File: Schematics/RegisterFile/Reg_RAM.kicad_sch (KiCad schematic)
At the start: 4 parts, among them U10 IS61WV6416DBLL-10TLI, U11 IS61WV6416DBLL-10TLI, U12 IS61WV6416DBLL-10TLI, U9 IS61WV6416DBLL-10TLI

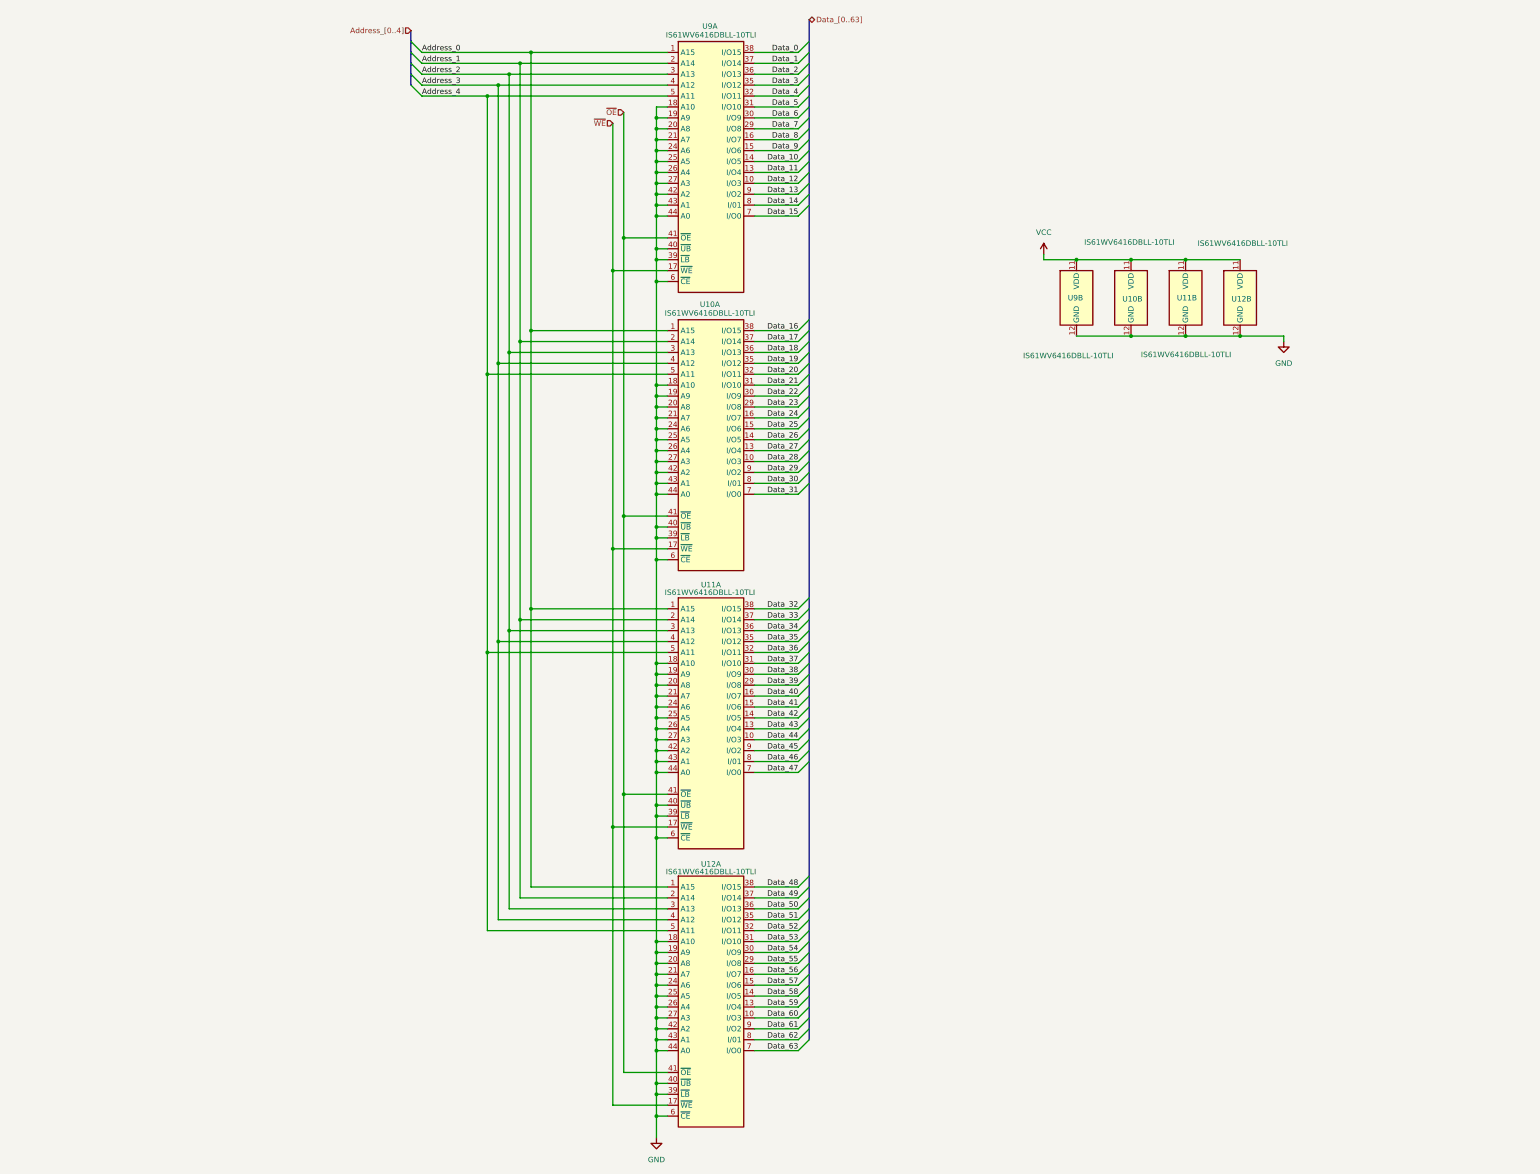
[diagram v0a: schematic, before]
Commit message: Updated RegFile diagrams + timing
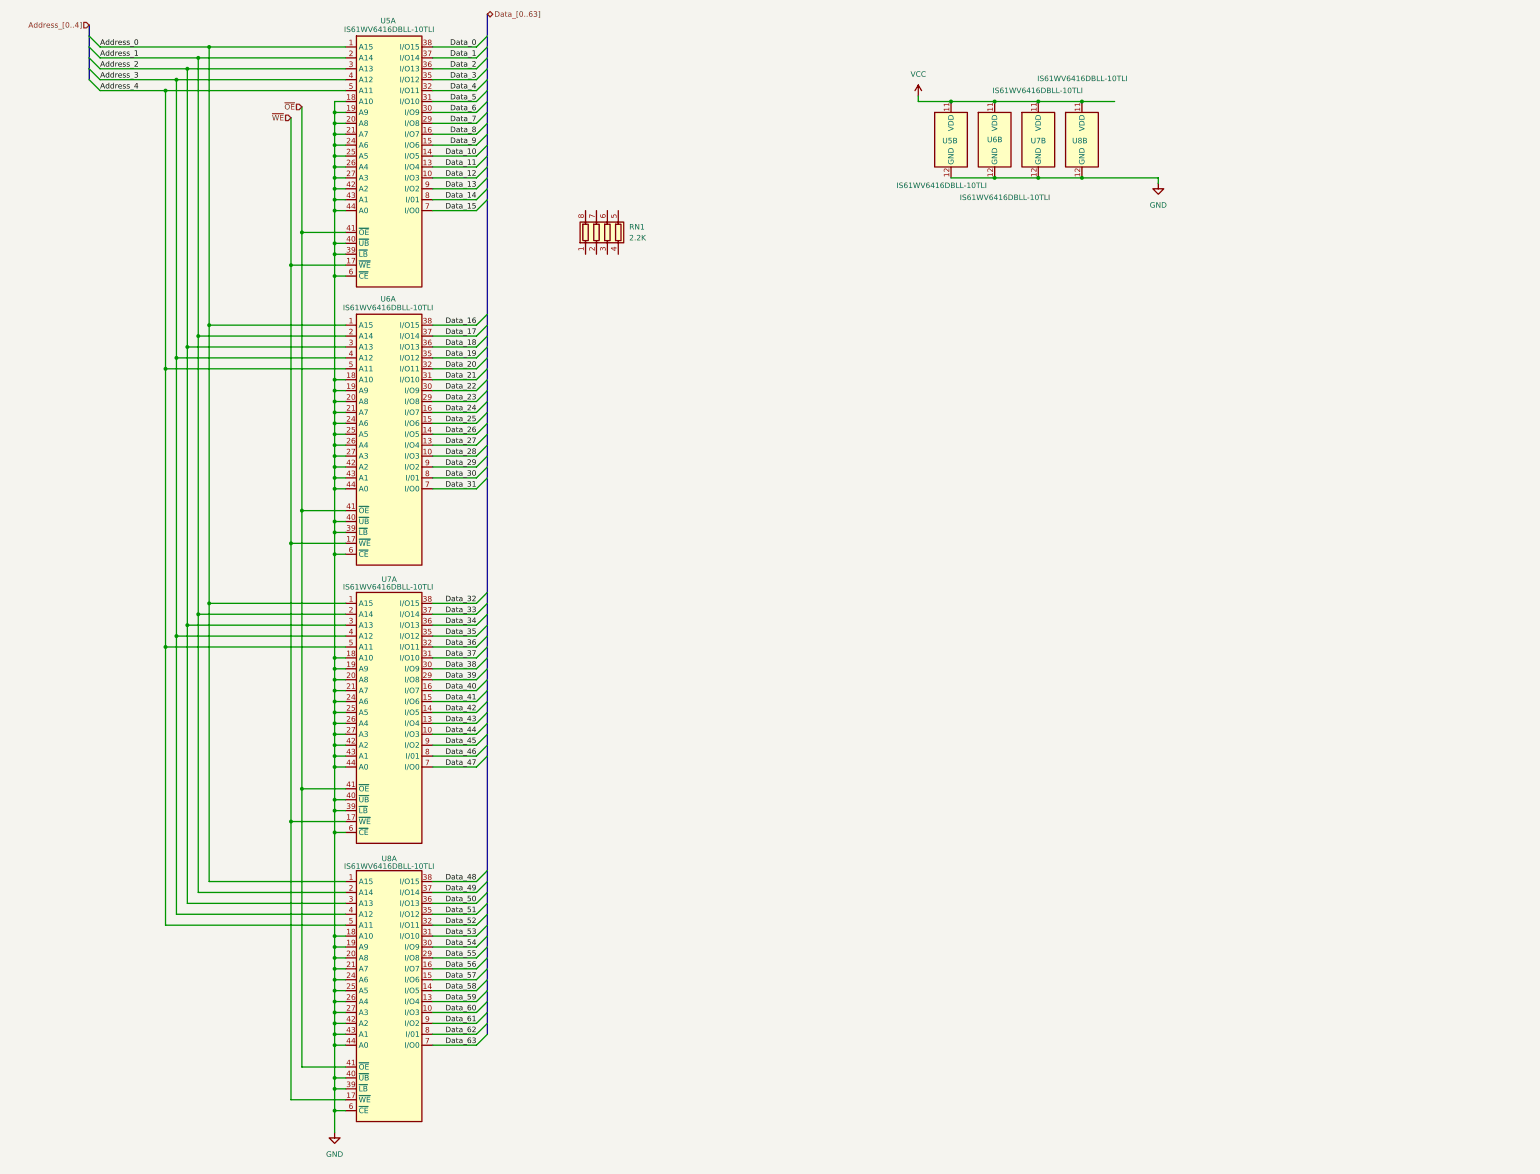
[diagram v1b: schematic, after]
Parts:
- removed unit 2 of U10
- removed unit 2 of U11
- removed unit 2 of U12
- removed unit 2 of U9
- added RN1: 2.2K, Package_DIP:DIP-6_W8.89mm_SMDSocket_LongPads, symbol Device:R_Pack04
- added unit 2 of U5
- added unit 2 of U6
- added unit 2 of U7
- added unit 2 of U8
- renumbered U9 to U5, U10 to U6, U11 to U7, U12 to U8
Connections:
- net GND: now also U5.12 (GND), U5.34 (GND), U6.12 (GND), U6.34 (GND), U7.12 (GND), U7.34 (GND), U8.12 (GND), U8.34 (GND)
- net VCC: now also U5.11 (VDD), U5.33 (VDD), U6.11 (VDD), U6.33 (VDD), U7.11 (VDD), U7.33 (VDD), U8.11 (VDD), U8.33 (VDD)
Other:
- moved on the sheet: U5A, U6A, U7A, U8A

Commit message: BIG UPDATE: Schematics, PCB & updated writeup for register
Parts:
- added C16, C17, C18, C19: 0.1uF, Capacitor_SMD:C_1206_3216Metric, symbol Device:C
- added RN18, RN19, RN20, RN21, RN22, RN23, RN24, RN25, RN26, RN27, RN28, RN29, RN30, RN31, RN32: 2.2K, Resistor_SMD:R_Array_Convex_4x0603, symbol Device:R_Pack04
- RN17: renamed from RN1; footprint Package_DIP:DIP-6_W8.89mm_SMDSocket_LongPads -> Resistor_SMD:R_Array_Convex_4x0603
- renumbered U5 to U12, U6 to U13, U7 to U14, U8 to U15
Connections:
- net Data_0: now also U12.16 (I/O7), RN25.5 (R4.2); no longer U12.38 (I/O15)
- net Data_1: now also U12.15 (I/O6), RN25.6 (R3.2); no longer U12.37 (I/O14)
- net Data_10: now also U12.31 (I/O10), RN21.7 (R2.2); no longer U12.14 (I/O5)
- net Data_11: now also U12.32 (I/O11), RN21.8 (R1.2); no longer U12.13 (I/O4)
- net Data_12: now also RN17.5 (R4.2), U12.35 (I/O12); no longer U12.10 (I/O3)
- net Data_13: now also RN17.6 (R3.2), U12.36 (I/O13); no longer U12.9 (I/O2)
- net Data_14: now also RN17.7 (R2.2), U12.37 (I/O14); no longer U12.8 (I/01)
- net Data_15: now also RN17.8 (R1.2), U12.38 (I/O15); no longer U12.7 (I/O0)
- net Data_16: now also U13.16 (I/O7), RN26.5 (R4.2); no longer U13.38 (I/O15)
- net Data_17: now also U13.15 (I/O6), RN26.6 (R3.2); no longer U13.37 (I/O14)
- net Data_18: now also U13.14 (I/O5), RN26.7 (R2.2); no longer U13.36 (I/O13)
- net Data_19: now also U13.13 (I/O4), RN26.8 (R1.2); no longer U13.35 (I/O12)
- net Data_2: now also U12.14 (I/O5), RN25.7 (R2.2); no longer U12.36 (I/O13)
- net Data_20: now also U13.10 (I/O3), RN30.5 (R4.2); no longer U13.32 (I/O11)
- net Data_21: now also U13.9 (I/O2), RN30.6 (R3.2); no longer U13.31 (I/O10)
- net Data_22: now also U13.8 (I/01), RN30.7 (R2.2); no longer U13.30 (I/O9)
- net Data_23: now also U13.7 (I/O0), RN30.8 (R1.2); no longer U13.29 (I/O8)
- net Data_24: now also U13.29 (I/O8), RN22.5 (R4.2); no longer U13.16 (I/O7)
- net Data_25: now also U13.30 (I/O9), RN22.6 (R3.2); no longer U13.15 (I/O6)
- net Data_26: now also U13.31 (I/O10), RN22.7 (R2.2); no longer U13.14 (I/O5)
- net Data_27: now also U13.32 (I/O11), RN22.8 (R1.2); no longer U13.13 (I/O4)
- net Data_28: now also U13.35 (I/O12), RN18.5 (R4.2); no longer U13.10 (I/O3)
- net Data_29: now also U13.36 (I/O13), RN18.6 (R3.2); no longer U13.9 (I/O2)
- net Data_3: now also U12.13 (I/O4), RN25.8 (R1.2); no longer U12.35 (I/O12)
- net Data_30: now also U13.37 (I/O14), RN18.7 (R2.2); no longer U13.8 (I/01)
- net Data_31: now also U13.38 (I/O15), RN18.8 (R1.2); no longer U13.7 (I/O0)
- net Data_32: now also U14.16 (I/O7), RN27.5 (R4.2); no longer U14.38 (I/O15)
- net Data_33: now also U14.15 (I/O6), RN27.6 (R3.2); no longer U14.37 (I/O14)
- net Data_34: now also U14.14 (I/O5), RN27.7 (R2.2); no longer U14.36 (I/O13)
- net Data_35: now also U14.13 (I/O4), RN27.8 (R1.2); no longer U14.35 (I/O12)
- net Data_36: now also U14.10 (I/O3), RN31.5 (R4.2); no longer U14.32 (I/O11)
- net Data_37: now also U14.9 (I/O2), RN31.6 (R3.2); no longer U14.31 (I/O10)
- net Data_38: now also U14.8 (I/01), RN31.7 (R2.2); no longer U14.30 (I/O9)
- net Data_39: now also U14.7 (I/O0), RN31.8 (R1.2); no longer U14.29 (I/O8)
- net Data_4: now also U12.10 (I/O3), RN29.5 (R4.2); no longer U12.32 (I/O11)
- net Data_40: now also U14.29 (I/O8), RN23.5 (R4.2); no longer U14.16 (I/O7)
- net Data_41: now also U14.30 (I/O9), RN23.6 (R3.2); no longer U14.15 (I/O6)
- net Data_42: now also U14.31 (I/O10), RN23.7 (R2.2); no longer U14.14 (I/O5)
- net Data_43: now also U14.32 (I/O11), RN23.8 (R1.2); no longer U14.13 (I/O4)
- net Data_44: now also U14.35 (I/O12), RN19.5 (R4.2); no longer U14.10 (I/O3)
- net Data_45: now also U14.36 (I/O13), RN19.6 (R3.2); no longer U14.9 (I/O2)
- net Data_46: now also U14.37 (I/O14), RN19.7 (R2.2); no longer U14.8 (I/01)
- net Data_47: now also U14.38 (I/O15), RN19.8 (R1.2); no longer U14.7 (I/O0)
- net Data_48: now also U15.16 (I/O7), RN28.5 (R4.2); no longer U15.38 (I/O15)
- net Data_49: now also U15.15 (I/O6), RN28.6 (R3.2); no longer U15.37 (I/O14)
- net Data_5: now also U12.9 (I/O2), RN29.6 (R3.2); no longer U12.31 (I/O10)
- net Data_50: now also U15.14 (I/O5), RN28.7 (R2.2); no longer U15.36 (I/O13)
- net Data_51: now also U15.13 (I/O4), RN28.8 (R1.2); no longer U15.35 (I/O12)
- net Data_52: now also U15.10 (I/O3), RN32.5 (R4.2); no longer U15.32 (I/O11)
- net Data_53: now also U15.9 (I/O2), RN32.6 (R3.2); no longer U15.31 (I/O10)
- net Data_54: now also U15.8 (I/01), RN32.7 (R2.2); no longer U15.30 (I/O9)
- net Data_55: now also U15.7 (I/O0), RN32.8 (R1.2); no longer U15.29 (I/O8)
- net Data_56: now also U15.29 (I/O8), RN24.5 (R4.2); no longer U15.16 (I/O7)
- net Data_57: now also U15.30 (I/O9), RN24.6 (R3.2); no longer U15.15 (I/O6)
- net Data_58: now also U15.31 (I/O10), RN24.7 (R2.2); no longer U15.14 (I/O5)
- net Data_59: now also U15.32 (I/O11), RN24.8 (R1.2); no longer U15.13 (I/O4)
- net Data_6: now also U12.8 (I/01), RN29.7 (R2.2); no longer U12.30 (I/O9)
- net Data_60: now also U15.35 (I/O12), RN20.5 (R4.2); no longer U15.10 (I/O3)
- net Data_61: now also U15.36 (I/O13), RN20.6 (R3.2); no longer U15.9 (I/O2)
- net Data_62: now also U15.37 (I/O14), RN20.7 (R2.2); no longer U15.8 (I/01)
- net Data_63: now also U15.38 (I/O15), RN20.8 (R1.2); no longer U15.7 (I/O0)
- net Data_7: now also U12.7 (I/O0), RN29.8 (R1.2); no longer U12.29 (I/O8)
- net Data_8: now also U12.29 (I/O8), RN21.5 (R4.2); no longer U12.16 (I/O7)
- net Data_9: now also U12.30 (I/O9), RN21.6 (R3.2); no longer U12.15 (I/O6)
- net GND: now also RN17.1 (R1.1), RN17.2 (R2.1), RN17.3 (R3.1), RN17.4 (R4.1), C16.2, C17.2, C18.2, C19.2, RN18.1 (R1.1), RN18.2 (R2.1), RN18.3 (R3.1), RN18.4 (R4.1), RN19.1 (R1.1), RN19.2 (R2.1), RN19.3 (R3.1), RN19.4 (R4.1), RN20.1 (R1.1), RN20.2 (R2.1), RN20.3 (R3.1), RN20.4 (R4.1), RN21.1 (R1.1), RN21.2 (R2.1), RN21.3 (R3.1), RN21.4 (R4.1), RN22.1 (R1.1), RN22.2 (R2.1), RN22.3 (R3.1), RN22.4 (R4.1), RN23.1 (R1.1), RN23.2 (R2.1), RN23.3 (R3.1), RN23.4 (R4.1), RN24.1 (R1.1), RN24.2 (R2.1), RN24.3 (R3.1), RN24.4 (R4.1), RN25.1 (R1.1), RN25.2 (R2.1), RN25.3 (R3.1), RN25.4 (R4.1), RN26.1 (R1.1), RN26.2 (R2.1), RN26.3 (R3.1), RN26.4 (R4.1), RN27.1 (R1.1), RN27.2 (R2.1), RN27.3 (R3.1), RN27.4 (R4.1), RN28.1 (R1.1), RN28.2 (R2.1), RN28.3 (R3.1), RN28.4 (R4.1), RN29.1 (R1.1), RN29.2 (R2.1), RN29.3 (R3.1), RN29.4 (R4.1), RN30.1 (R1.1), RN30.2 (R2.1), RN30.3 (R3.1), RN30.4 (R4.1), RN31.1 (R1.1), RN31.2 (R2.1), RN31.3 (R3.1), RN31.4 (R4.1), RN32.1 (R1.1), RN32.2 (R2.1), RN32.3 (R3.1), RN32.4 (R4.1)
- net VCC: now also C16.1, C17.1, C18.1, C19.1
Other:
- note added: "Decoupling Capacitors"
- moved on the sheet: RN17, U12B, U13B, U14B, U15B
